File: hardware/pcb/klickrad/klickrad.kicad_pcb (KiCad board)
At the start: 2 copper layers, 32 x 32 mm, 31 parts, among them J1 SM06B-SRSS-TB, SW1 B3U-1000P, U1 MPR121QR2, U2 DRV2605LDGSR

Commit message: Klickrad-Platine: Zwischenstand (in Arbeit)
Co-Authored-By: Claude Opus 5.5 <noreply@anthropic.com>
Claude-Session: https://claude.ai/code/session_01JifvE6gExGmwsJWDpfRrrS
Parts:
- removed H (x3): M2, MountingHole_2.2mm_NPTH
- removed R4: 10k, R_0402_1005Metric
- added H1: M2, Klickrad:MountingHole_2.2mm_NPTH, F.Cu at (100.0, 85.4)
- added H2: M2, Klickrad:MountingHole_2.2mm_NPTH, F.Cu at (87.4, 107.3)
- added H3: M2, Klickrad:MountingHole_2.2mm_NPTH, F.Cu at (112.6, 107.3)
- C1, C2, C3, C4, C5: footprint C_0402_1005Metric -> Capacitor_SMD:C_0402_1005Metric
- C6: footprint C_0603_1608Metric -> Capacitor_SMD:C_0603_1608Metric
- J1: footprint JST_SH_SM06B-SRSS-TB_1x06-1MP_P1.00mm_Horizontal -> Connector_JST:JST_SH_SM06B-SRSS-TB_1x06-1MP_P1.00mm_Horizontal
- R1, R2, R3: footprint R_0402_1005Metric -> Resistor_SMD:R_0402_1005Metric
- SEG1: footprint SEG1 -> Klickrad:SEG1
- SEG10: footprint SEG10 -> Klickrad:SEG10
- SEG11: footprint SEG11 -> Klickrad:SEG11
- SEG12: footprint SEG12 -> Klickrad:SEG12
- SEG2: footprint SEG2 -> Klickrad:SEG2
- SEG3: footprint SEG3 -> Klickrad:SEG3
- SEG4: footprint SEG4 -> Klickrad:SEG4
- SEG5: footprint SEG5 -> Klickrad:SEG5
- SEG6: footprint SEG6 -> Klickrad:SEG6
- SEG7: footprint SEG7 -> Klickrad:SEG7
- SEG8: footprint SEG8 -> Klickrad:SEG8
- SEG9: footprint SEG9 -> Klickrad:SEG9
- SW1: footprint SW_SPST_B3U-1000P -> Button_Switch_SMD:SW_SPST_B3U-1000P
- TP1, TP2: footprint SolderWirePad_1x01_SMD_1x2mm -> Connector_Wire:SolderWirePad_1x01_SMD_1x2mm
- U1: footprint QFN-20_3x3mm_P0.4mm_noEP -> Klickrad:QFN-20_3x3mm_P0.4mm_noEP
- U2: footprint MSOP-10_3x3mm_P0.5mm -> Package_SO:MSOP-10_3x3mm_P0.5mm
- moved TP1 12.7 mm to (87.7, 103.0), turned to -90 degrees
- moved TP2 12.3 mm to (87.7, 100.4), turned to -90 degrees
- moved C4 12.0 mm to (89.8, 106.3), turned to -90 degrees
- moved C6 10.7 mm to (90.0, 103.9), turned to -90 degrees
- moved C5 9.77 mm to (92.8, 106.6)
- moved R2 7.16 mm to (101.5, 107.0)
- moved R3 4.75 mm to (101.2, 104.6)
- moved C3 4.39 mm to (103.0, 103.2)
- moved C2 3.77 mm to (98.0, 103.2), turned to -90 degrees
- moved C1 3.50 mm to (103.0, 101.8)
- moved R1 3.34 mm to (96.8, 100.8)
- moved U2 1.39 mm to (91.9, 108.5)
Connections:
- SEG1 pad 1: ELE0 -> ELE8
- SEG10 pad 1: ELE9 -> ELE11
- SEG12 pad 1: ELE11 -> ELE9
- SEG2 pad 1: ELE1 -> ELE7
- SEG3 pad 1: ELE2 -> ELE6
- SEG4 pad 1: ELE3 -> ELE5
- SEG6 pad 1: ELE5 -> ELE3
- SEG7 pad 1: ELE6 -> ELE2
- SEG8 pad 1: ELE7 -> ELE1
- SEG9 pad 1: ELE8 -> ELE0
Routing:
- net GND: track 0.00 -> 29.7 mm, vias 0 -> 9
- net 3V3: track 0.00 -> 26.9 mm, vias 0 -> 5
- net SDA: track 0.00 -> 20.9 mm, vias 0 -> 2
- net SCL: track 0.00 -> 18.5 mm
- net LRA_N: track 0.00 -> 15.6 mm
- net LRA_P: track 0.00 -> 11.8 mm
- net ELE0: track 0.00 -> 11.4 mm, vias 0 -> 1
- net ELE1: track 0.00 -> 10.0 mm, vias 0 -> 1
- net BTN: track 0.00 -> 9.76 mm, vias 0 -> 1
- net INT: track 0.00 -> 9.54 mm, vias 0 -> 2
- net ELE11: track 0.00 -> 9.26 mm, vias 0 -> 1
- net ELE2: track 0.00 -> 8.68 mm, vias 0 -> 1
- net ELE10: track 0.00 -> 8.32 mm, vias 0 -> 1
- net ELE3: track 0.00 -> 8.26 mm, vias 0 -> 1
- net ELE4: track 0.00 -> 7.37 mm, vias 0 -> 1
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- added copper zone on In2.Cu, net 3V3
- added copper zone on In1.Cu, net GND
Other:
- copper layers 2 -> 4
- board text added: "0 Grad"
- board text added: "3V3"
- board text added: "BTN"
- board text added: "GND"
- board text added: "INT"
- board text added: "KLICKRAD v1"
- board text added: "LRA 6x16 aufkleben"
- board text added: "LRA+"
- board text added: "LRA-"
- board text added: "SCL"
- board text added: "SDA"

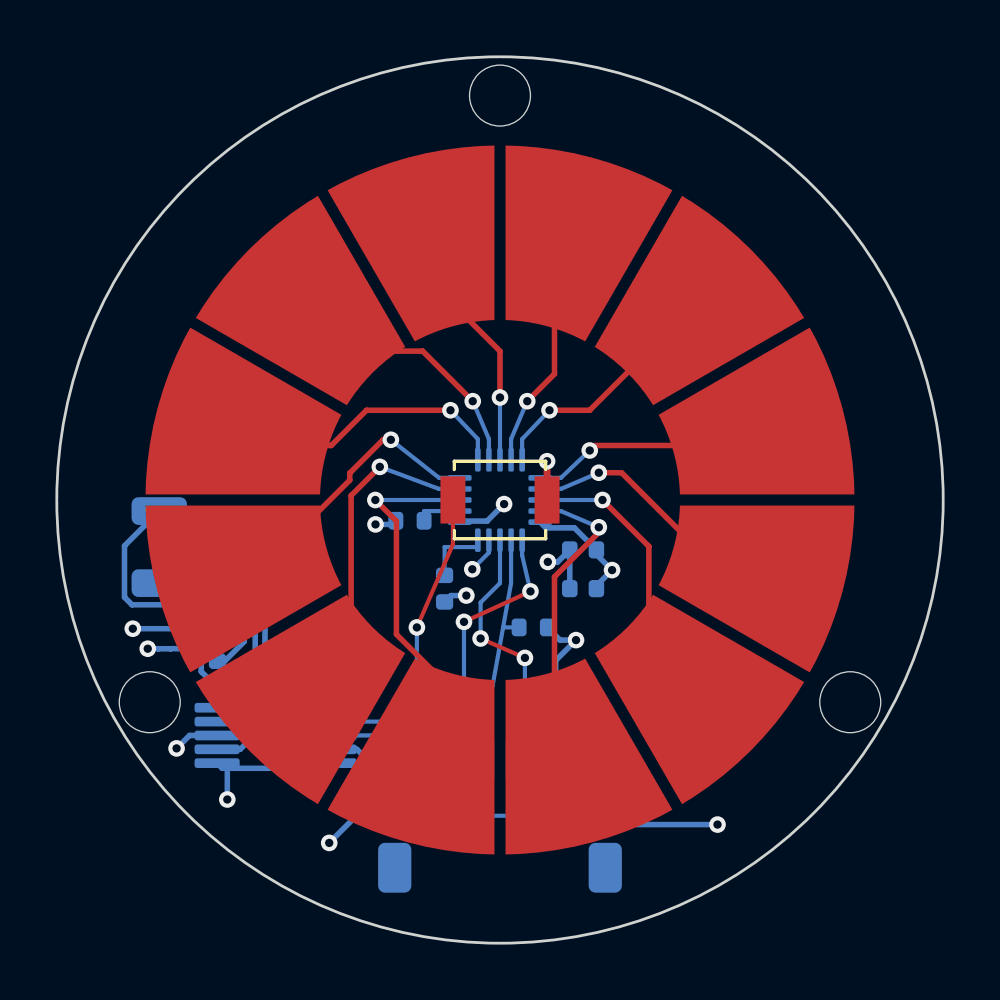
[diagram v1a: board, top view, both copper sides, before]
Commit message: Zwischenstand vor Pause: Klickrad v2 und Hauptplatine (unvollständig)
Beide Pakete wurden auf Wunsch angehalten. Klickrad v1 (MPR121) ist der
letzte fertige Stand der Klickrad-Platine in der Historie.

Co-Authored-By: Claude Opus 5.5 <noreply@anthropic.com>
Claude-Session: https://claude.ai/code/session_01JifvE6gExGmwsJWDpfRrrS
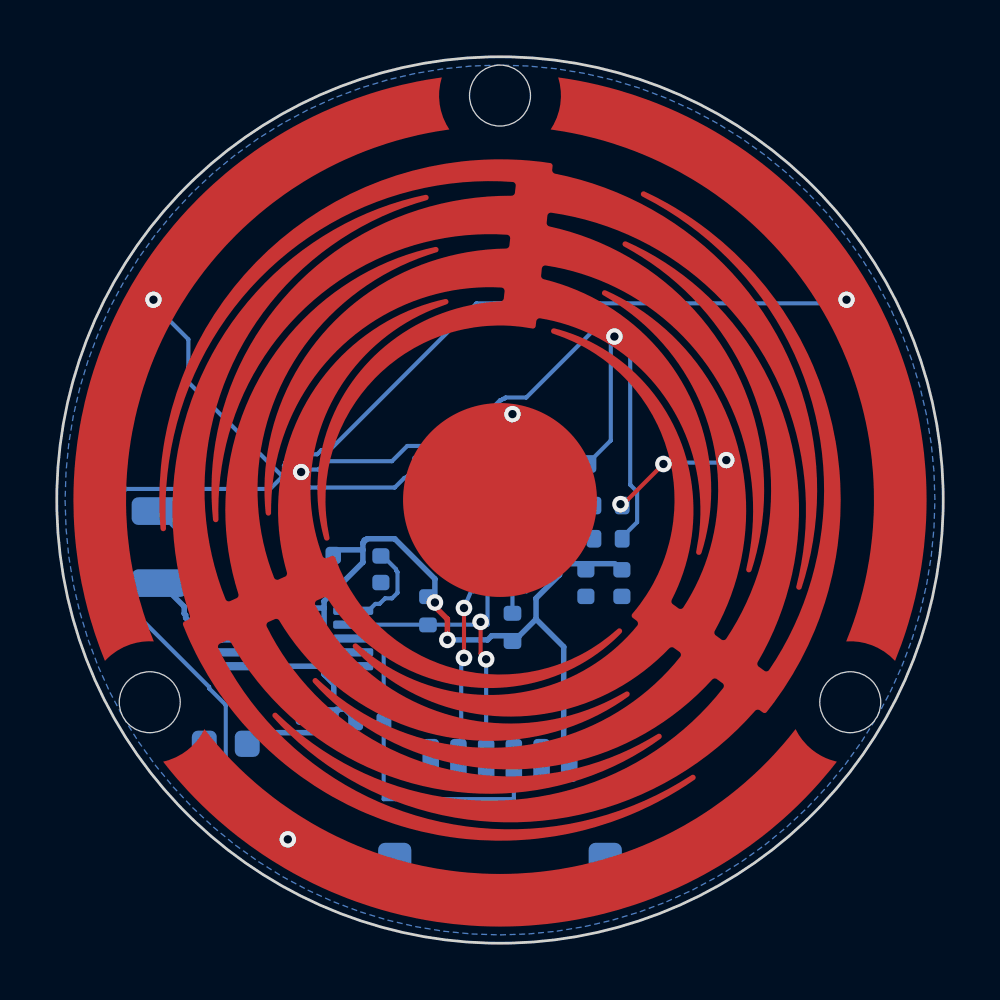
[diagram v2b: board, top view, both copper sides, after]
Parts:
- removed C6: 10uF, Capacitor_SMD:C_0603_1608Metric
- removed SEG1: Touch1, Klickrad:SEG1
- removed SEG10: Touch10, Klickrad:SEG10
- removed SEG11: Touch11, Klickrad:SEG11
- removed SEG12: Touch12, Klickrad:SEG12
- removed SEG2: Touch2, Klickrad:SEG2
- removed SEG3: Touch3, Klickrad:SEG3
- removed SEG4: Touch4, Klickrad:SEG4
- removed SEG5: Touch5, Klickrad:SEG5
- removed SEG6: Touch6, Klickrad:SEG6
- removed SEG7: Touch7, Klickrad:SEG7
- removed SEG8: Touch8, Klickrad:SEG8
- removed SEG9: Touch9, Klickrad:SEG9
- added R4: 10k, Resistor_SMD:R_0402_1005Metric, B.Cu at (100.5, 98.2)
- added R5: 10k, Resistor_SMD:R_0402_1005Metric, B.Cu at (97.6, 98.7)
- added R6: 10k, Resistor_SMD:R_0402_1005Metric, B.Cu at (100.5, 104.6)
- added R7: 10k, Resistor_SMD:R_0402_1005Metric, B.Cu at (93.4, 107.8)
- added R8: 4.7k, Resistor_SMD:R_0402_1005Metric, B.Cu at (95.3, 108.0)
- added R9: 4.7k, Resistor_SMD:R_0402_1005Metric, B.Cu at (97.4, 104.0)
- added SW2: WHEEL, Klickrad:qtouch-wheel, F.Cu at (100.0, 100.0)
- added SW3: GUARD, Klickrad:qtouch-guard, F.Cu at (100.0, 100.0)
- C2: value 0.1uF -> 1uF
- C5: value 1uF -> 10uF; footprint Capacitor_SMD:C_0402_1005Metric -> Capacitor_SMD:C_0603_1608Metric
- R1: value 75k -> 10k
- R2, R3: value 4.7k -> 10k
- SW1: value B3U-1000P -> BUTTON; footprint Button_Switch_SMD:SW_SPST_B3U-1000P -> Klickrad:qtouch-button
- U1: value MPR121QR2 -> AT42QT2120; footprint Klickrad:QFN-20_3x3mm_P0.4mm_noEP -> Package_DFN_QFN:VQFN-20-1EP_3x3mm_P0.45mm_EP1.55x1.55mm
- U2: footprint Package_SO:MSOP-10_3x3mm_P0.5mm -> Package_SO:VSSOP-10_3x3mm_P0.5mm
- moved C3 9.58 mm to (93.5, 102.0)
- moved R2 7.21 mm to (103.9, 100.2), turned to 0 degrees
- moved R1 7.18 mm to (103.9, 101.4), turned to 0 degrees
- moved C4 7.02 mm to (95.7, 102.5)
- moved C2 6.40 mm to (104.4, 103.0)
- moved R3 6.09 mm to (102.7, 98.7), turned to 0 degrees
- moved U2 3.55 mm to (92.5, 105.0)
- moved C5 3.48 mm to (90.1, 108.8)
- moved U1 1.50 mm to (100.0, 101.5), turned to -90 degrees
- moved C1 1.20 mm to (103.1, 103.0), turned to -90 degrees
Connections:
- net REXT renamed K0
- C2 pad 1: VREG -> 3V3
- C4 pad 1: 3V3 -> REG
- C5 pad 1: REG -> 3V3
- J1 pad 5: INT -> CHANGE
- J1 pad 6: BTN -> unconnected-(J1-Pin_6-Pad6)
- R1 pad 2: GND -> E0
- R2 pad 1: 3V3 -> K1
- R2 pad 2: SDA -> E1
- R3 pad 1: 3V3 -> K2
- R3 pad 2: SCL -> E2
- SW1 pad 1: BTN -> EB
- U1 pad 1: INT -> unconnected-(U1-KEY6-Pad1)
- U1 pad 10: ELE2 -> GND
- U1 pad 11: ELE3 -> SDA
- U1 pad 12: ELE4 -> RESET
- U1 pad 13: ELE5 -> unconnected-(U1-NC-Pad13)
- U1 pad 14: ELE6 -> SCL
- U1 pad 15: ELE7 -> CHANGE
- U1 pad 16: ELE8 -> unconnected-(U1-KEY11-Pad16)
- U1 pad 17: ELE9 -> unconnected-(U1-KEY10-Pad17)
- U1 pad 18: ELE10 -> unconnected-(U1-KEY9-Pad18)
- U1 pad 19: ELE11 -> unconnected-(U1-KEY8-Pad19)
- U1 pad 2: SCL -> unconnected-(U1-KEY5-Pad2)
- U1 pad 20: 3V3 -> unconnected-(U1-KEY7-Pad20)
- U1 pad 3: SDA -> KG
- U1 pad 4: 3V3 -> KB
- U1 pad 5: VREG -> K2
- U1 pad 6: GND -> K1
- U1 pad 8: ELE0 -> GND
- U1 pad 9: ELE1 -> 3V3
- U2 pad 5: 3V3 -> EN
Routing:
- net EG: track 0.00 -> 57.0 mm, vias 0 -> 3
- net GND: track 29.7 -> 0.00 mm, vias 9 -> 0
- net E0: track 0.00 -> 21.6 mm, vias 0 -> 1
- net ELE0: track 11.4 -> 0.00 mm, vias 1 -> 0
- net LRA_N: track 15.6 -> 4.37 mm
- net ELE1: track 10.0 -> 0.00 mm, vias 1 -> 0
- net BTN: track 9.76 -> 0.00 mm, vias 1 -> 0
- net INT: track 9.54 -> 0.00 mm, vias 2 -> 0
- net ELE11: track 9.26 -> 0.00 mm, vias 1 -> 0
- net 3V3: track 26.9 -> 36.1 mm, vias 5 -> 2
- net LRA_P: track 11.8 -> 2.82 mm
- net ELE2: track 8.68 -> 0.00 mm, vias 1 -> 0
- net SDA: track 20.9 -> 12.5 mm, vias 2 -> 0
- net ELE10: track 8.32 -> 0.00 mm, vias 1 -> 0
- net ELE3: track 8.26 -> 0.00 mm, vias 1 -> 0
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- added copper zone on B.Cu, net GND
- removed copper zone on In2.Cu, net 3V3
- removed copper zone on In1.Cu, net GND
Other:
- copper layers 4 -> 2
- board text added: "(6)"
- board text added: "CHG"
- board text added: "KLICKRAD v2"
- board text added: "OBEN"
- board text added: "QT2120 0x1C DRV 0x5A"
- board text removed: "BTN"
- board text removed: "INT"
- board text removed: "KLICKRAD v1"

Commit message: Platinen: Zwischenstand (in Arbeit)
Co-Authored-By: Claude Opus 5.5 <noreply@anthropic.com>
Claude-Session: https://claude.ai/code/session_01JifvE6gExGmwsJWDpfRrrS
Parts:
- J1: value SM06B-SRSS-TB -> FH12-6S-0.5SH; footprint Connector_JST:JST_SH_SM06B-SRSS-TB_1x06-1MP_P1.00mm_Horizontal -> Connector_FFC-FPC:Hirose_FH12-6S-0.5SH_1x06-1MP_P0.50mm_Horizontal
- moved R8 2.70 mm to (97.4, 106.3), turned to 180 degrees
- moved R7 2.06 mm to (95.2, 106.8)
- moved R9 1.20 mm to (97.4, 105.2), turned to 180 degrees
- moved J1 0.60 mm to (100.0, 110.8)
- moved C4 0.50 mm to (96.1, 102.2)
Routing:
- net EG: track 57.0 -> 11.3 mm, vias 3 -> 1
- net CHANGE: track 5.63 -> 34.9 mm, vias 2 -> 0
- net E0: track 21.6 -> 14.2 mm, vias 1 -> 3
- net SCL: track 10.5 -> 15.8 mm, vias 2 -> 3
- net 3V3: track 36.1 -> 34.8 mm
- net REG: track 2.47 -> 2.79 mm, vias 0 -> 2
- net E1: track 4.22 -> 3.91 mm, vias 3 -> 1
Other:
- board text added: "LRA 6x12 aufkleben"
- board text removed: "LRA 6x16 aufkleben"

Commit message: Hauptplatine: platziert, nicht geroutet; Befund in KONZEPT.md
Co-Authored-By: Claude Sonnet 5.5 <noreply@anthropic.com>
Claude-Session: https://claude.ai/code/session_01JifvE6gExGmwsJWDpfRrrS
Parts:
- removed C5: 10uF, Capacitor_SMD:C_0603_1608Metric
- J1: value FH12-6S-0.5SH -> 503480-0600; footprint Connector_FFC-FPC:Hirose_FH12-6S-0.5SH_1x06-1MP_P0.50mm_Horizontal -> Klickrad:Molex_503480-0600_1x06-1MP_P0.50mm_Horizontal
- moved TP2 25.8 mm to (113.1, 104.8)
- moved TP1 25.4 mm to (113.1, 102.4)
- moved C3 17.6 mm to (110.2, 107.6), turned to 0 degrees
- moved U2 16.1 mm to (108.5, 103.6), turned to 0 degrees
- moved R7 12.7 mm to (106.4, 100.8), turned to -90 degrees
- moved C4 9.30 mm to (104.5, 106.2)
- moved C1 2.06 mm to (102.6, 105.0)
- moved C2 1.95 mm to (102.6, 103.7), turned to 90 degrees
- moved R9 1.70 mm to (98.7, 106.3), turned to 0 degrees
- moved R4 1.66 mm to (101.9, 99.0), turned to 0 degrees
- moved R3 1.32 mm to (102.9, 100.0)
- moved R5 1.02 mm to (97.4, 99.7)
- moved R1 0.90 mm to (104.8, 101.4)
- moved R2 0.90 mm to (104.8, 100.2)
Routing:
- net GND: track 0.00 -> 33.4 mm, vias 0 -> 2
- net CHANGE: track 34.9 -> 8.69 mm
- net SDA: track 12.1 -> 17.0 mm, vias 0 -> 3
- net SCL: track 15.8 -> 12.4 mm
- net LRA_N: track 4.16 -> 0.88 mm
- net 3V3: track 34.8 -> 37.9 mm, vias 2 -> 4
- net EB: track 0.45 -> 3.43 mm
- net LRA_P: track 2.82 -> 0.88 mm
- net REG: track 2.79 -> 1.25 mm, vias 2 -> 0
- net EG: track 11.3 -> 12.6 mm
- net E2: track 4.40 -> 5.62 mm
- net K0: track 1.44 -> 2.36 mm
- net K1: track 1.46 -> 2.36 mm
- net EN: track 0.45 -> 1.05 mm
- added copper zone on F.Cu, net GND
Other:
- board text added: "LRA bis 3 mm hoch: 12x6 / 16x6"
- board text removed: "LRA 6x12 aufkleben"

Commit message: Klickrad v2 und S31-Test: Zwischenstand (in Arbeit)
Co-Authored-By: Claude Sonnet 5.5 <noreply@anthropic.com>
Claude-Session: https://claude.ai/code/session_01JifvE6gExGmwsJWDpfRrrS
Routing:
- net SCL: track 12.4 -> 21.8 mm, vias 3 -> 4
- net 3V3: track 37.9 -> 32.1 mm, vias 4 -> 0
- net GND: track 33.4 -> 31.5 mm, vias 2 -> 1
- net CHANGE: track 8.69 -> 9.75 mm
- net SDA: track 17.0 -> 16.0 mm

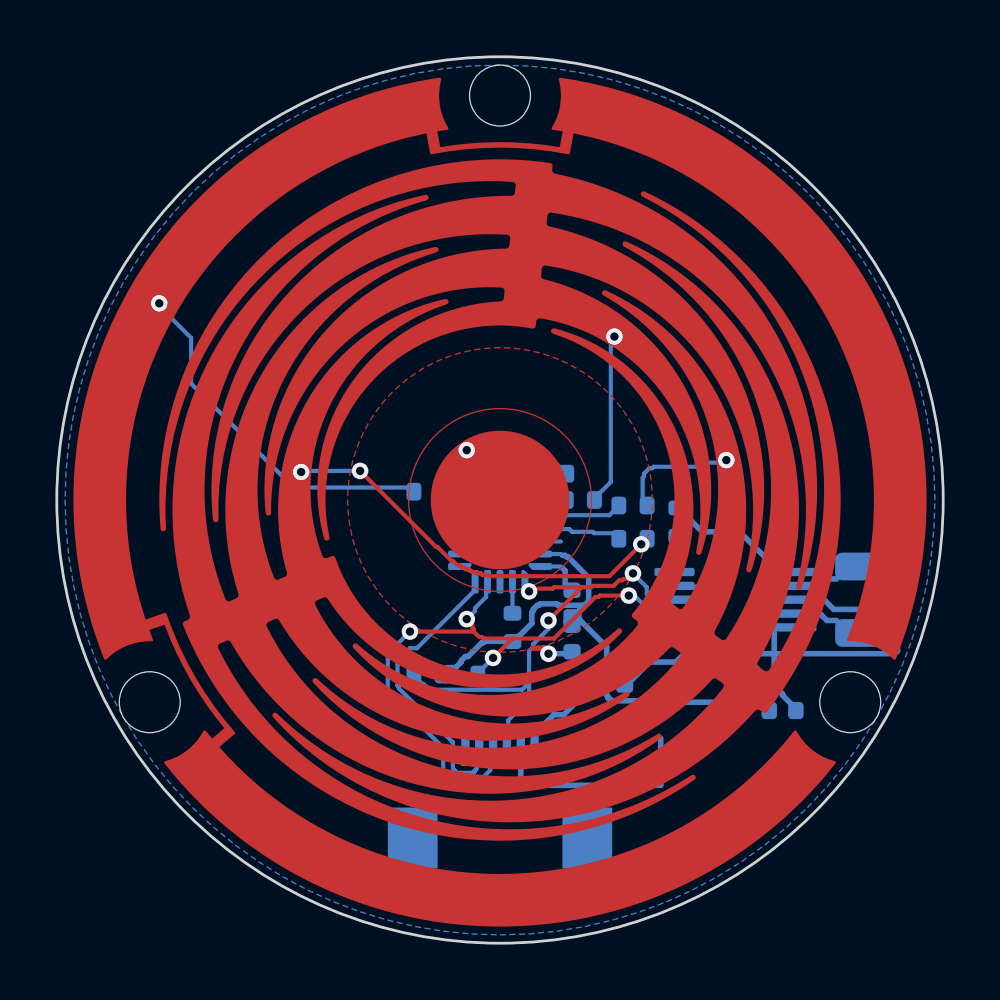
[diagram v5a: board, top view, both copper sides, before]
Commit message: S31-Buildtest-Ergebnis und offene Punkte dokumentiert
Co-Authored-By: Claude Sonnet 5.5 <noreply@anthropic.com>
Claude-Session: https://claude.ai/code/session_01JifvE6gExGmwsJWDpfRrrS
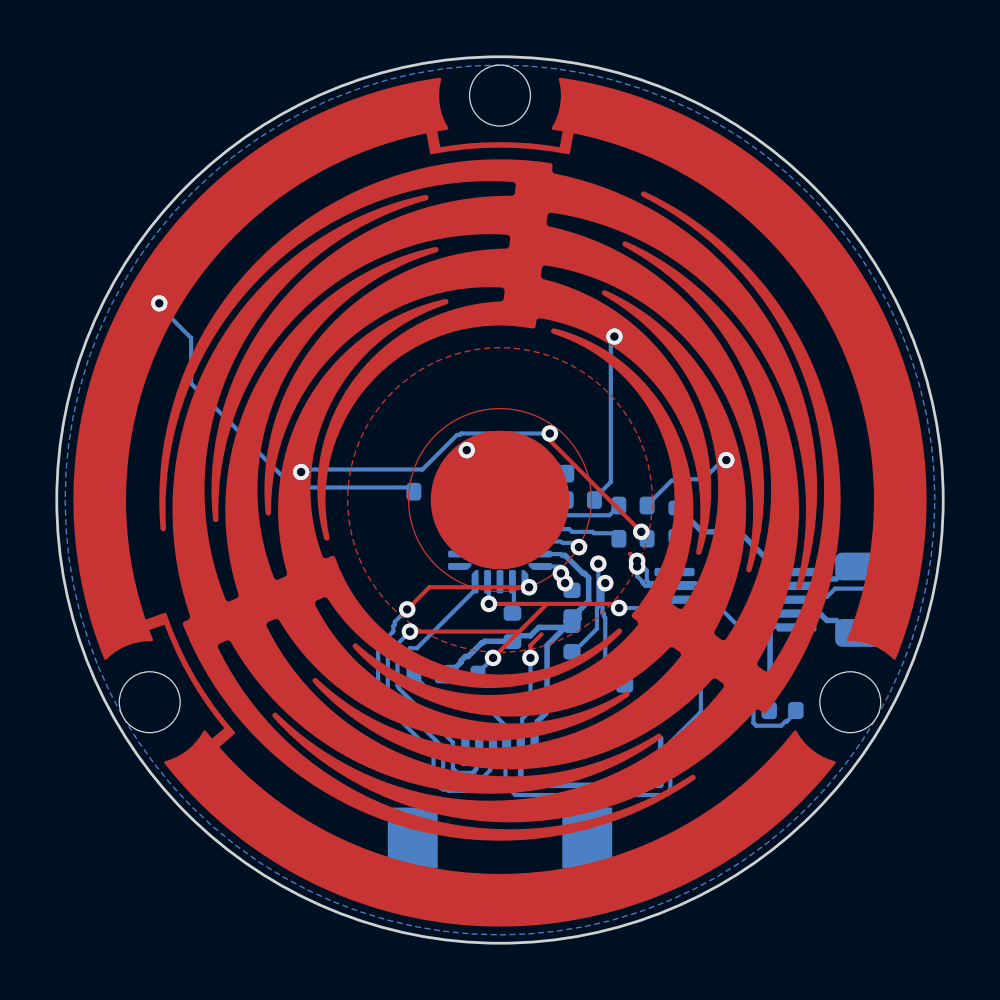
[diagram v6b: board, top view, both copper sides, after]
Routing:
- net SDA: track 16.0 -> 34.8 mm, vias 3 -> 2
- net 3V3: track 32.1 -> 23.2 mm
- net GND: track 31.5 -> 39.1 mm, vias 1 -> 8
- net E1: track 3.84 -> 3.01 mm
- net SCL: track 21.8 -> 22.4 mm

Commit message: Zwischenstand Klickrad v2 und Hauptplatine
Co-Authored-By: Claude Sonnet 5.5 <noreply@anthropic.com>
Claude-Session: https://claude.ai/code/session_01JifvE6gExGmwsJWDpfRrrS
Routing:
- net GND: track 39.1 -> 38.0 mm, vias 8 -> 5
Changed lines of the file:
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@@
-		(net 13)
-	)
-	(via
-		(at 102.35 103)
-		(size 0.6)
-		(drill 0.3)
-		(layers "F.Cu" "B.Cu")
-		(net 13)
-	)
-	(via
-		(at 104.95 102.4)
-		(size 0.6)
-		(drill 0.3)
-		(layers "F.Cu" "B.Cu")
-		(net 13)
-	)
-	(via
-		(at 103.55 102.3)
-		(size 0.6)
-		(drill 0.3)
-		(layers "F.Cu" "B.Cu")
 		(net 13)
 	)
@@
 	)
 	(segment
-		(start 114.3 101.7)
-		(end 114.3 101.65)
-		(width 0.15)
-		(layer "B.Cu")
-		(net 13)
-	)
-	(segment
 		(start 101.45 101.5)
 		(end 102.2 101.5)
@@
 	)
 	(segment
-		(start 114.35 101.75)
-		(end 114.3 101.7)
-		(width 0.15)
-		(layer "B.Cu")
-		(net 13)
-	)
-	(segment
 		(start 103.8 104.25)
 		(end 103.75 104.2)
@@
 		(width 0.15)
 		(layer "B.Cu")
-		(net 13)
-	)
-	(segment
-		(start 114.3 101.65)
-		(end 113.6 100.95)
-		(width 0.15)
-		(layer "B.Cu")

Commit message: Klickrad v2 fertig: TEILE.md und Problemliste aktualisiert
Co-Authored-By: Claude Sonnet 5.5 <noreply@anthropic.com>
Claude-Session: https://claude.ai/code/session_01JifvE6gExGmwsJWDpfRrrS
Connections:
- U1 pad 21: (no net) -> GND
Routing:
- net 3V3: track 23.2 -> 43.7 mm, vias 0 -> 2
- net SDA: track 34.8 -> 14.6 mm, vias 2 -> 3
- net GND: track 38.0 -> 32.2 mm, vias 5 -> 3
- net LRA_N: track 0.88 -> 2.72 mm
- net LRA_P: track 0.88 -> 2.72 mm
- net SCL: track 22.4 -> 21.8 mm
